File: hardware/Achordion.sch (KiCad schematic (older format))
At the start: 87 parts, among them J1 Power, J10 Jack, J11 Jack, J4 Jack, J5 Jack, J6 Jack, J7 Jack, J8 Jack, J9 Jack, SW2 Button, U4 LM4040C10, U6 TL072, U7 MCP6002, U8 MCP6002, U9 MCP6002

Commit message: Add CV probing
Follow mutable instruments pattern and add a normalization probe. This
probe will send pseudo random sequence. When this sequence is detected
on input, we know the jack is not plugged.

Signed-off-by: Petr Horacek <hrck@protonmail.com>
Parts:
- removed J10, J11, J4, J5, J6, J7, J8, J9: Jack, Connector_Audio:Jack_3.5mm_QingPu_WQP-PJ398SM_Vertical_CircularHoles, symbol Connector:AudioJack2
- added D11: BAT54S, Package_TO_SOT_SMD:SOT-23, symbol Diode:BAT54S
- added J10, J11, J4, J5, J6, J7, J8, J9: Jack, Connector_Audio:Jack_3.5mm_QingPu_WQP-PJ398SM_Vertical_CircularHoles, symbol Connector:AudioJack2_SwitchT
- added R43, R45, R46, R47, R48, R49: 10k, Resistor_SMD:R_0603_1608Metric, symbol Device:R_Small
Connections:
- net labels added: PROBE
- wire segments 298 -> 322
- no-connect marks 14 -> 15
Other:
- moved on the sheet: C46, C47, C48, U7C, U8C, U9C

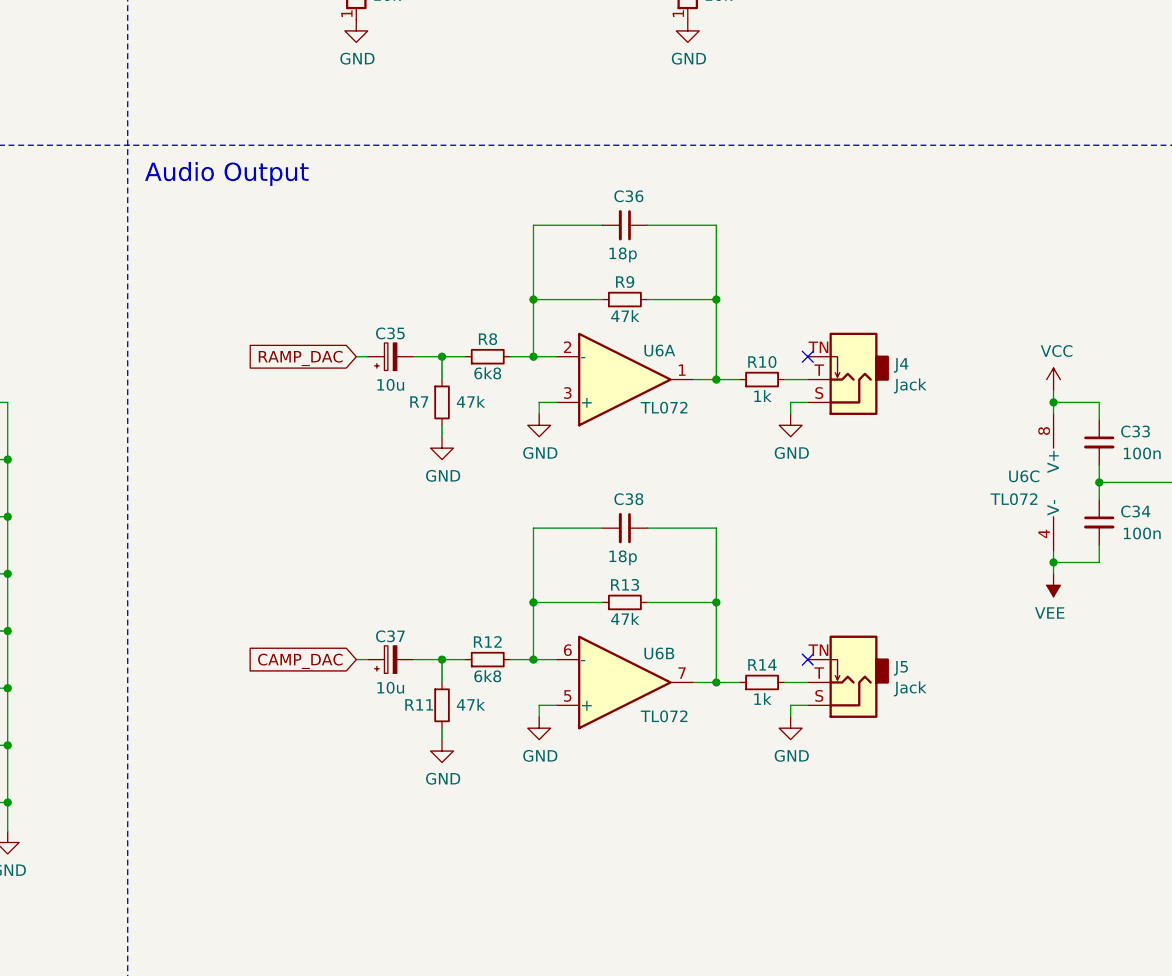
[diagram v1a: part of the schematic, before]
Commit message: Mix outputs when only one jack is plugged
Following Mutable Instrument's Rings.

Signed-off-by: Petr Horacek <hrck@protonmail.com>
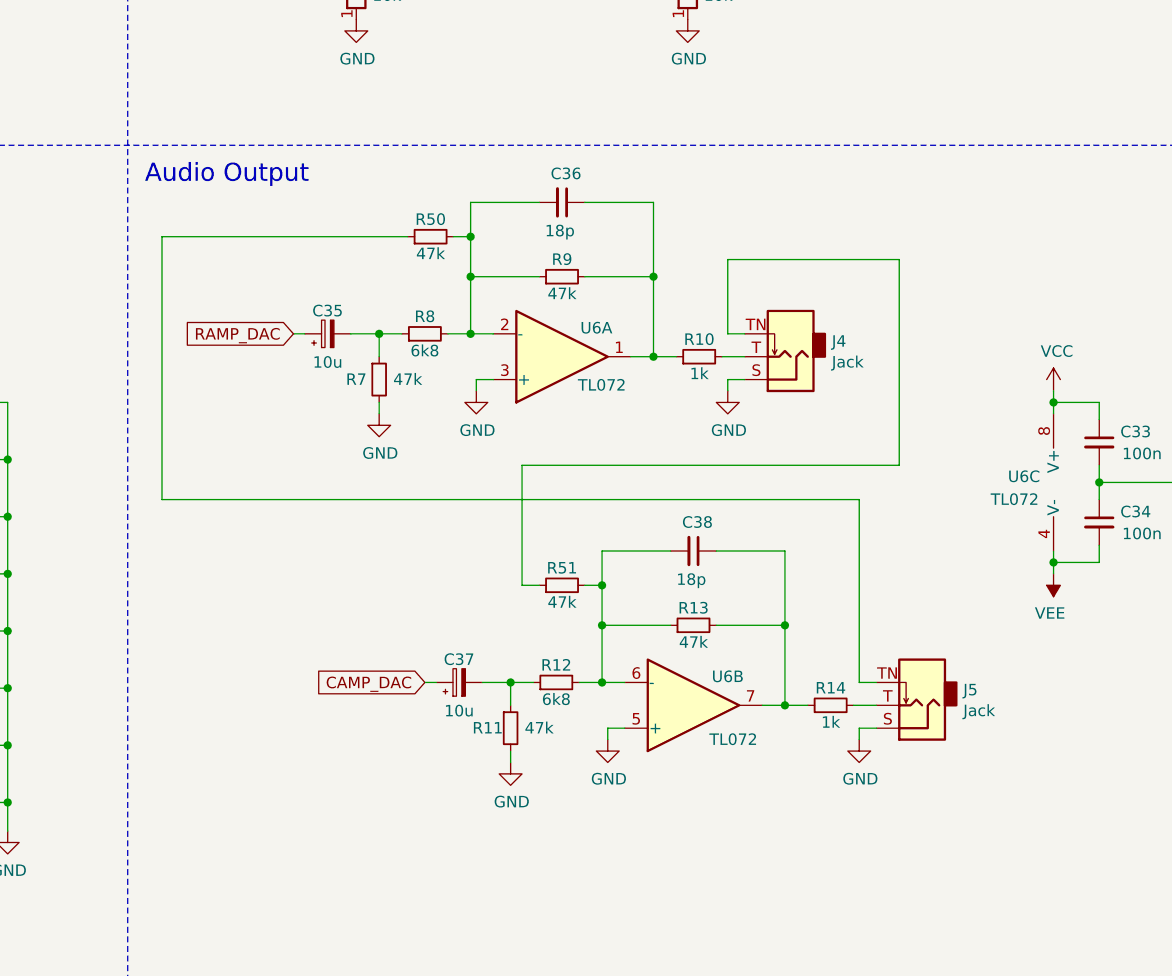
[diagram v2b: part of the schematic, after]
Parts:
- added R50, R51: 47k, Resistor_SMD:R_0603_1608Metric, symbol Device:R_Small
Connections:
- net at J5.TN: now also R50.1
- net at J4.TN: now also R51.1
- net at C36.2, R8.2, R9.1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: now also R50.2
- net at C38.2, R12.2, R13.1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: now also R51.2
- no-connect marks 15 -> 13
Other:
- moved on the sheet: C35, C36, C37, C38, J4, J5, R10, R11, R12, R13, R14, R7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

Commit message: Add schottky and LEDs to BOM
Signed-off-by: Petr Horacek <hrck@protonmail.com>
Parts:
- D10, D3, D4, D5, D6, D7, D8, D9: Mfr Part Number (none) -> WP710A10SRD/D
- D11: Mfr Part Number (none) -> BAT54S,215
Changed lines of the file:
@@
 F 2 "LED_THT:LED_D3.0mm" V 10150 8075 50  0001 C CNN
 F 3 "~" V 10150 8075 50  0001 C CNN
+F 4 "WP710A10SRD/D" H 10150 8075 50  0001 C CNN "Mfr Part Number"
 	1    10150 8075
 	-1   0    0    1
@@
 F 2 "LED_THT:LED_D3.0mm" V 10150 8325 50  0001 C CNN
 F 3 "~" V 10150 8325 50  0001 C CNN
+F 4 "WP710A10SRD/D" H 10150 8325 50  0001 C CNN "Mfr Part Number"
 	1    10150 8325
 	-1   0    0    1
@@
 F 2 "LED_THT:LED_D3.0mm" V 10150 8575 50  0001 C CNN
 F 3 "~" V 10150 8575 50  0001 C CNN
+F 4 "WP710A10SRD/D" H 10150 8575 50  0001 C CNN "Mfr Part Number"
 	1    10150 8575
 	-1   0    0    1
@@
 F 2 "LED_THT:LED_D3.0mm" V 10150 8825 50  0001 C CNN
 F 3 "~" V 10150 8825 50  0001 C CNN
+F 4 "WP710A10SRD/D" H 10150 8825 50  0001 C CNN "Mfr Part Number"
 	1    10150 8825
 	-1   0    0    1
@@
 F 2 "LED_THT:LED_D3.0mm" V 10150 9075 50  0001 C CNN
 F 3 "~" V 10150 9075 50  0001 C CNN
+F 4 "WP710A10SRD/D" H 10150 9075 50  0001 C CNN "Mfr Part Number"
 	1    10150 9075
 	-1   0    0    1
@@
 F 2 "LED_THT:LED_D3.0mm" V 10150 9325 50  0001 C CNN
 F 3 "~" V 10150 9325 50  0001 C CNN
+F 4 "WP710A10SRD/D" H 10150 9325 50  0001 C CNN "Mfr Part Number"
 	1    10150 9325
 	-1   0    0    1
@@
 F 2 "LED_THT:LED_D3.0mm" V 10150 9575 50  0001 C CNN
 F 3 "~" V 10150 9575 50  0001 C CNN
+F 4 "WP710A10SRD/D" H 10150 9575 50  0001 C CNN "Mfr Part Number"
 	1    10150 9575
 	-1   0    0    1
@@
 F 2 "LED_THT:LED_D3.0mm" V 10150 9825 50  0001 C CNN
 F 3 "~" V 10150 9825 50  0001 C CNN
+F 4 "WP710A10SRD/D" H 10150 9825 50  0001 C CNN "Mfr Part Number"
 	1    10150 9825
 	-1   0    0    1
@@
 F 2 "Package_TO_SOT_SMD:SOT-23" H 1475 10725 50  0001 L CNN
 F 3 "https://www.diodes.com/assets/Datasheets/ds11005.pdf" H 1280 10600 50  0001 C CNN
+F 4 "BAT54S,215" H 1400 10600 50  0001 C CNN "Mfr Part Number"
 	1    1400 10600
 	0    1    -1   0

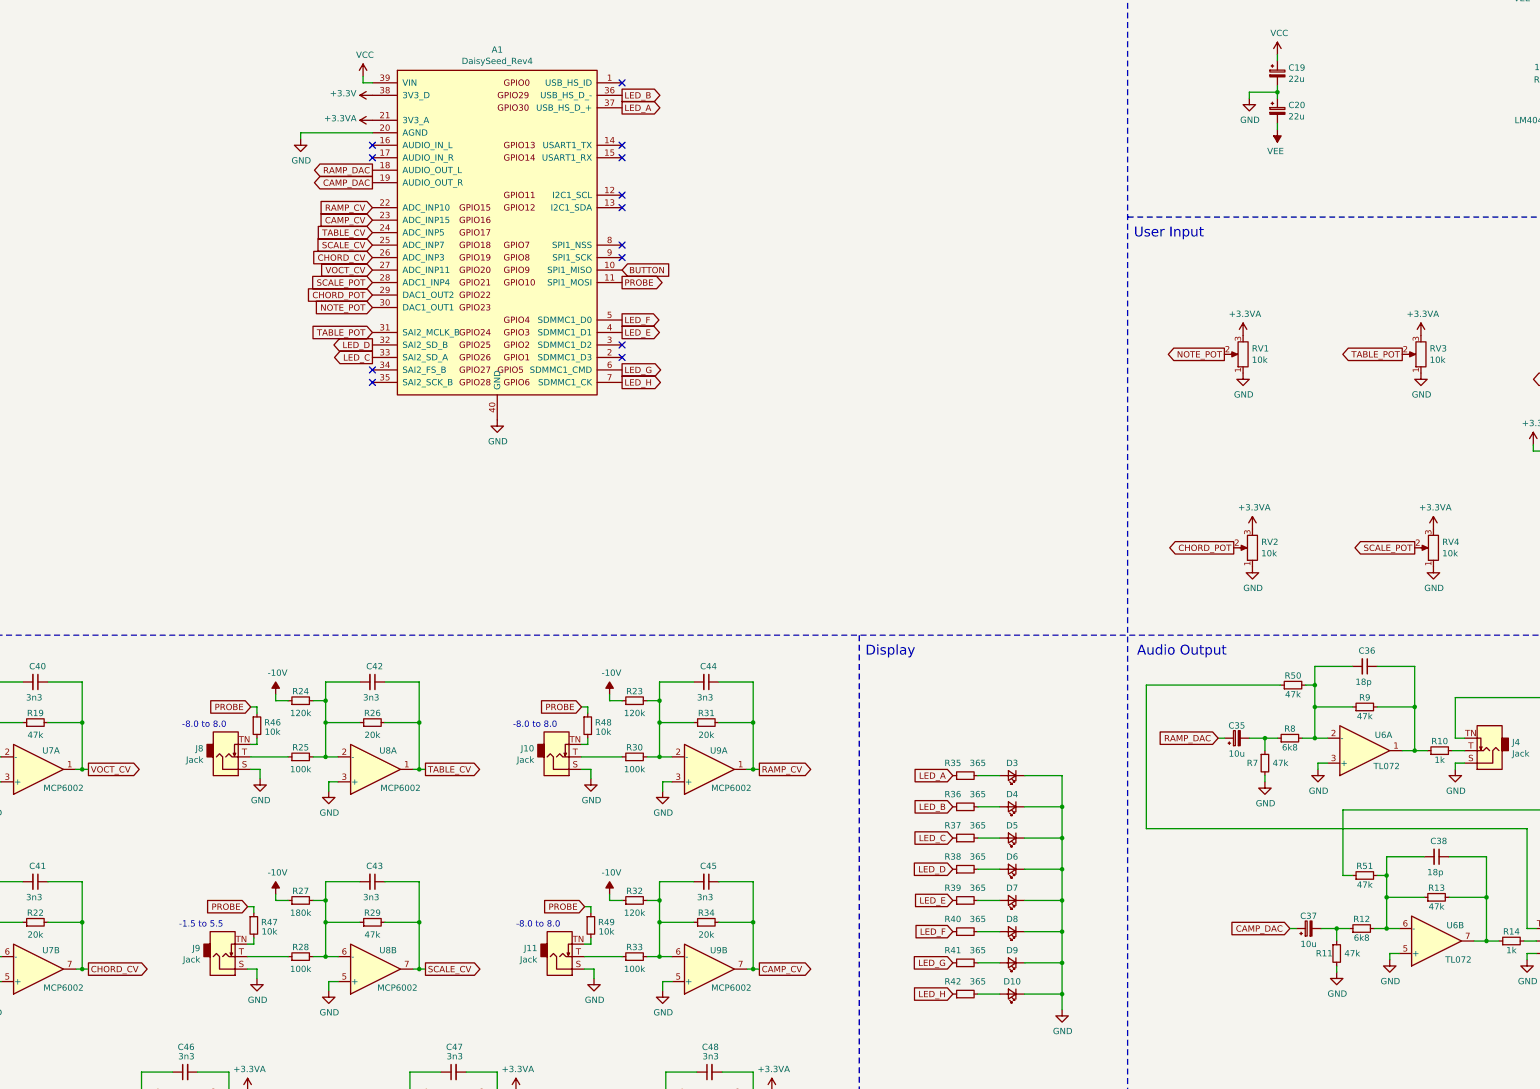
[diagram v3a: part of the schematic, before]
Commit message: Index all peripherals and label them on PCB
Signed-off-by: Petr Horacek <hrck@protonmail.com>
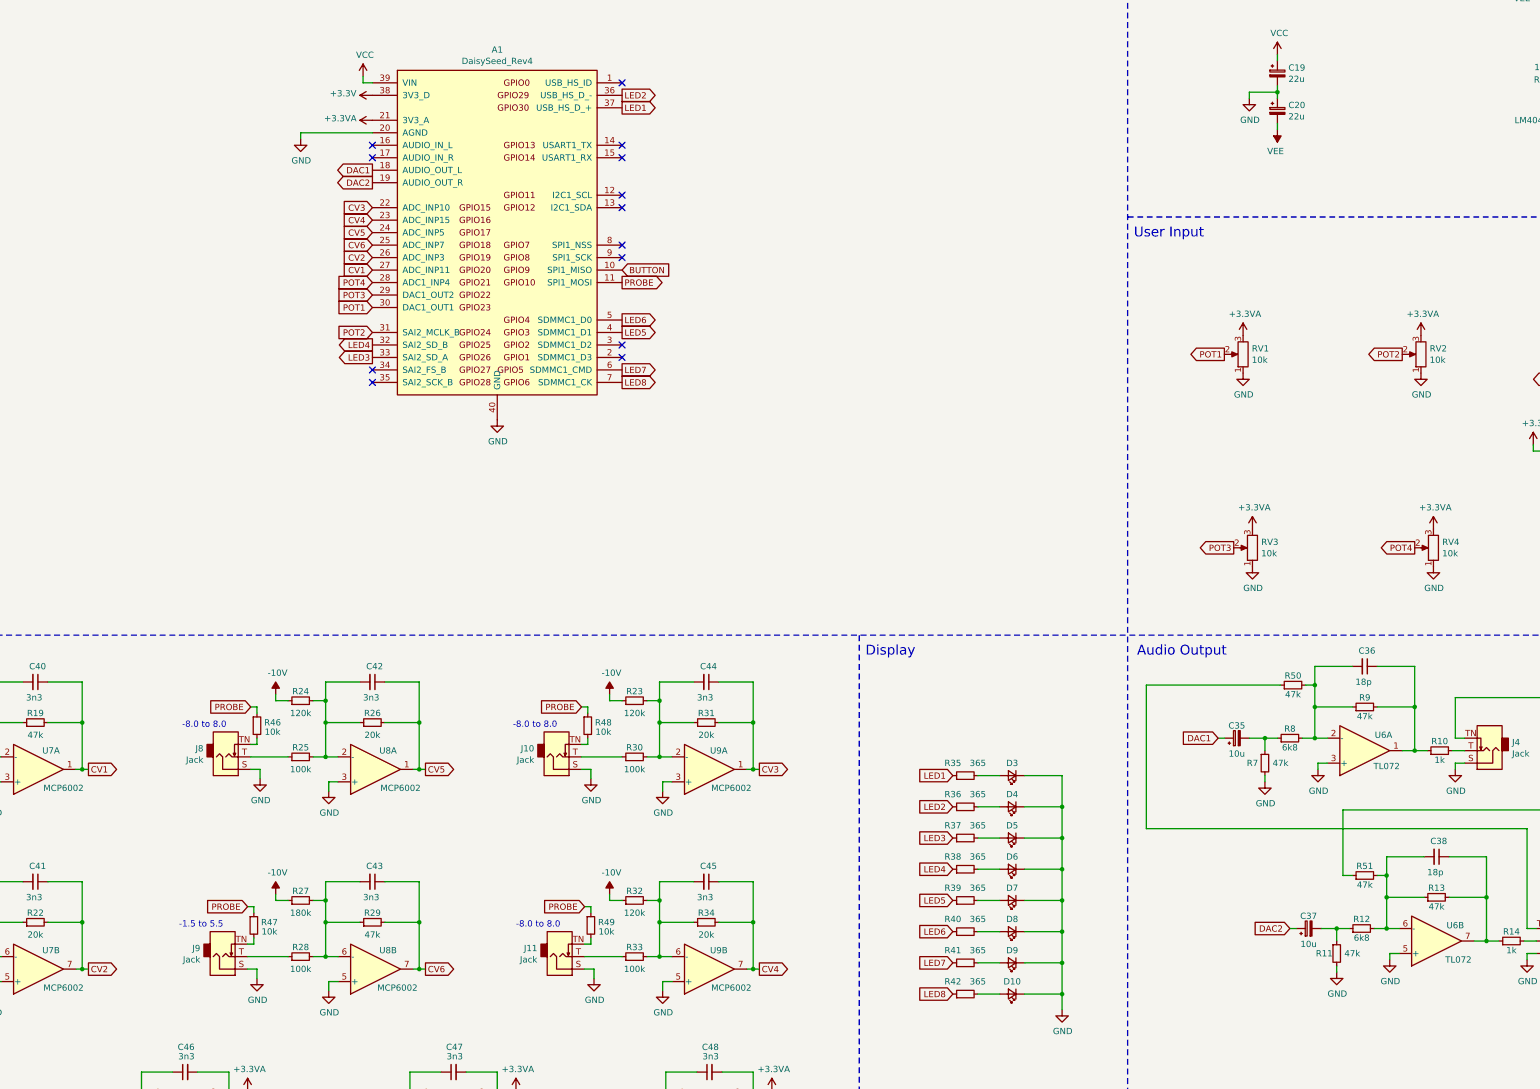
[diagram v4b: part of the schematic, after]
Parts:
- renumbered RV3 to RV2, RV2 to RV3
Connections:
- net CAMP_CV renamed CV4
- net CAMP_DAC renamed DAC2
- net CHORD_CV renamed CV2
- net CHORD_POT renamed POT3
- net LED_A renamed LED1
- net LED_B renamed LED2
- net LED_C renamed LED3
- net LED_D renamed LED4
- net LED_E renamed LED5
- net LED_F renamed LED6
- net LED_G renamed LED7
- net LED_H renamed LED8
- net NOTE_POT renamed POT1
- net RAMP_CV renamed CV3
- net RAMP_DAC renamed DAC1
- net SCALE_CV renamed CV6
- net SCALE_POT renamed POT4
- net TABLE_CV renamed CV5
- net TABLE_POT renamed POT2
- net VOCT_CV renamed CV1

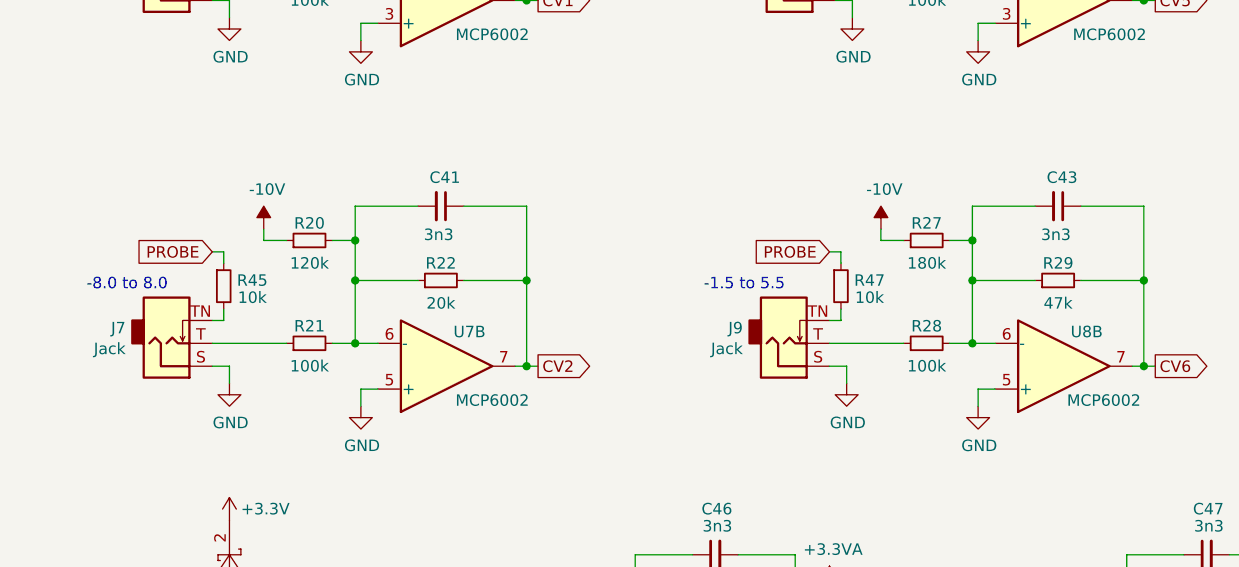
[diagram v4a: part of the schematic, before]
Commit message: Adjust CV ranges
V/OCT and Tonic will be driven by V/OCT limited to a smaller range in
the mostly positive section for increased accuracy. The rest would be -8
to 8 volts.

Signed-off-by: Petr Horacek <hrck@protonmail.com>
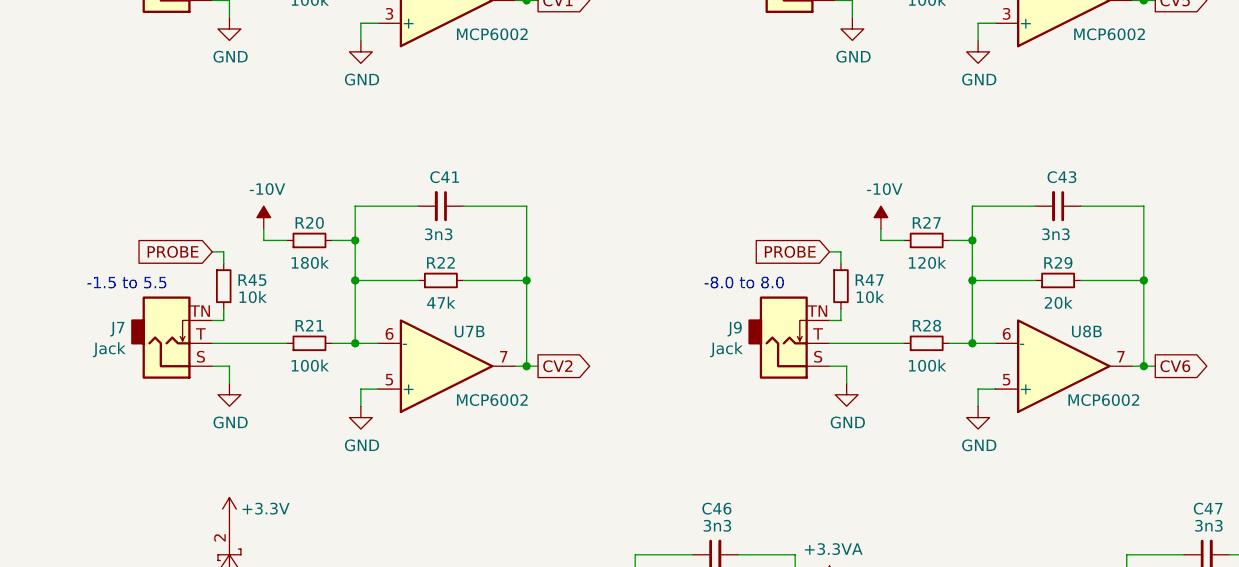
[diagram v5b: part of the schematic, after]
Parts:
- R20: value 120k -> 180k
- R22: value 20k -> 47k
- R27: value 180k -> 120k
- R29: value 47k -> 20k
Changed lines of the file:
@@
 P 1750 9075
 F 0 "R20" V 1825 9075 50  0000 C CNN
-F 1 "120k" V 1650 9075 50  0000 C CNN
+F 1 "180k" V 1650 9075 50  0000 C CNN
 F 2 "Resistor_SMD:R_0603_1608Metric" H 1750 9075 50  0001 C CNN
 F 3 "~" H 1750 9075 50  0001 C CNN
@@
 P 2325 9250
 F 0 "R22" V 2400 9250 50  0000 C CNN
-F 1 "20k" V 2225 9250 50  0000 C CNN
+F 1 "47k" V 2225 9250 50  0000 C CNN
 F 2 "Resistor_SMD:R_0603_1608Metric" H 2325 9250 50  0001 C CNN
 F 3 "~" H 2325 9250 50  0001 C CNN
@@
 P 5025 9250
 F 0 "R29" V 5100 9250 50  0000 C CNN
-F 1 "47k" V 4925 9250 50  0000 C CNN
+F 1 "20k" V 4925 9250 50  0000 C CNN
 F 2 "Resistor_SMD:R_0603_1608Metric" H 5025 9250 50  0001 C CNN
 F 3 "~" H 5025 9250 50  0001 C CNN
@@
 P 4450 9075
 F 0 "R27" V 4525 9075 50  0000 C CNN
-F 1 "180k" V 4350 9075 50  0000 C CNN
+F 1 "120k" V 4350 9075 50  0000 C CNN
 F 2 "Resistor_SMD:R_0603_1608Metric" H 4450 9075 50  0001 C CNN
 F 3 "~" H 4450 9075 50  0001 C CNN
@@
 $EndComp
 Text Notes 3475 9300 0    50   ~ 0
--1.5 to 5.5
+-8.0 to 8.0
 Text GLabel 5450 9625 2    50   Output ~ 0
 CV6
@@
 $EndComp
 Text Notes 775  9300 0    50   ~ 0
--8.0 to 8.0
+-1.5 to 5.5
 Text Notes 775  7700 0    50   ~ 0
 -1.5 to 5.5

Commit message: Use bigger pads in PCB
Make hand soldering easier.

Signed-off-by: Petr Horacek <hrck@protonmail.com>
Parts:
- C19, C20: footprint Capacitor_Tantalum_SMD:CP_EIA-3528-21_Kemet-B -> Capacitor_Tantalum_SMD:CP_EIA-3528-21_Kemet-B_Pad1.50x2.35mm_HandSolder
- C21: footprint Capacitor_SMD:C_1206_3216Metric -> Capacitor_SMD:C_1206_3216Metric_Pad1.33x1.80mm_HandSolder
- C33, C34, C36, C38, C39, C40, C41, C42, C43, C44, C45, C46, C47, C48: footprint Capacitor_SMD:C_0603_1608Metric -> Capacitor_SMD:C_0603_1608Metric_Pad1.08x0.95mm_HandSolder
- C35, C37: footprint Capacitor_Tantalum_SMD:CP_EIA-3216-18_Kemet-A -> Capacitor_Tantalum_SMD:CP_EIA-3216-18_Kemet-A_Pad1.58x1.35mm_HandSolder
- D11, U4: footprint Package_TO_SOT_SMD:SOT-23 -> Package_TO_SOT_SMD:SOT-23_Handsoldering
- R10, R11, R12, R13, R14, R15, R16, R17, R18, R19, R20, R21, R22, R23, R24, R25, R26, R27, R28, R29, R30, R31, R32, R33, R34, R35, R36, R37, R38, R39, R4, R40, R41, R42, R43, R45, R46, R47, R48, R49, R5, R50, R51, R7, R8, R9: footprint Resistor_SMD:R_0603_1608Metric -> Resistor_SMD:R_0603_1608Metric_Pad0.98x0.95mm_HandSolder
